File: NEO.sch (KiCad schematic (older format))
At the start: 13 parts, among them Q601 2N7002BKT, U601 U-BLOX-NEO-M8N, X601 ANT

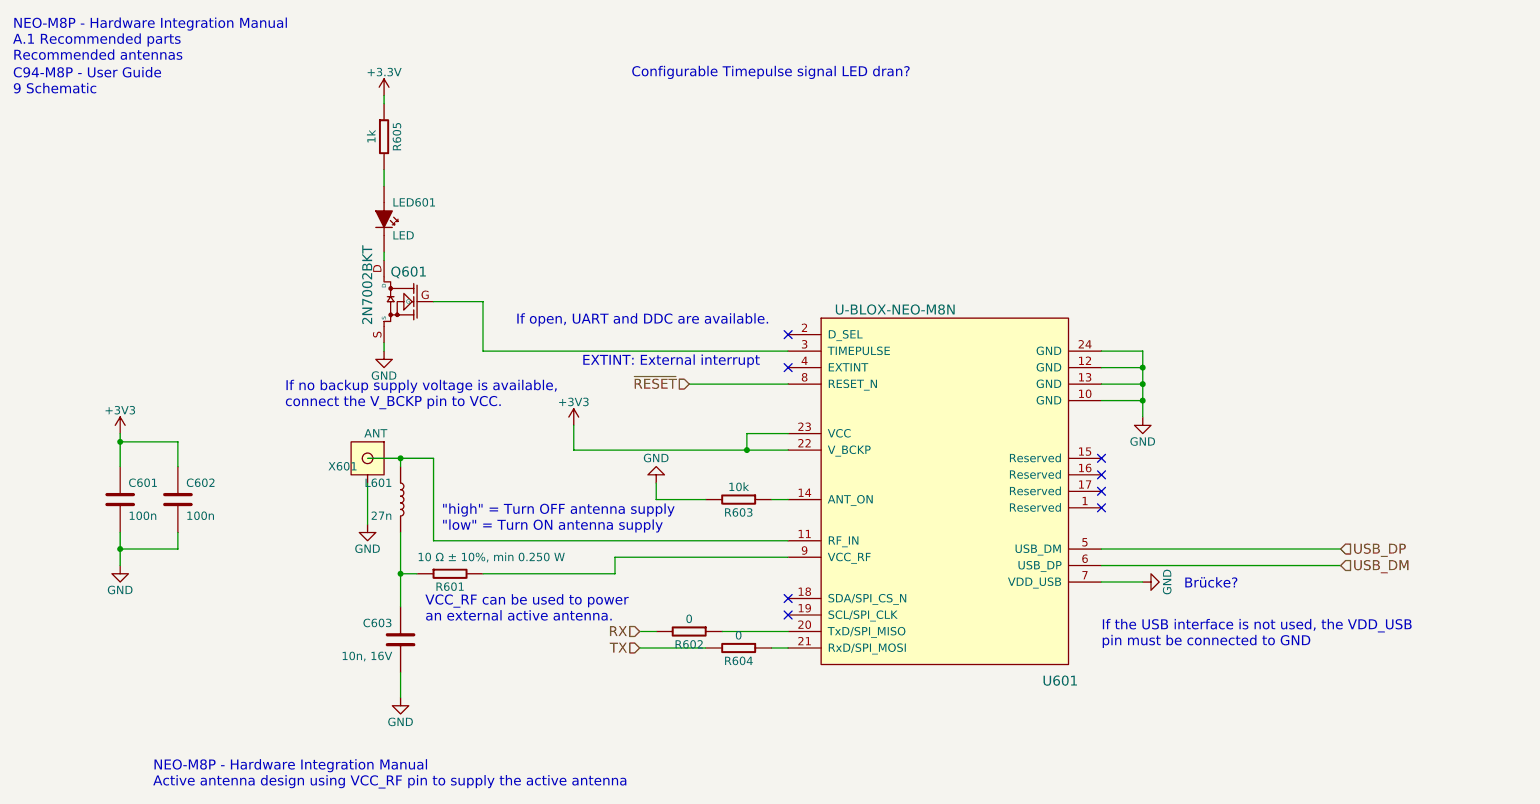
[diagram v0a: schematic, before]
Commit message: adjusted 3d models
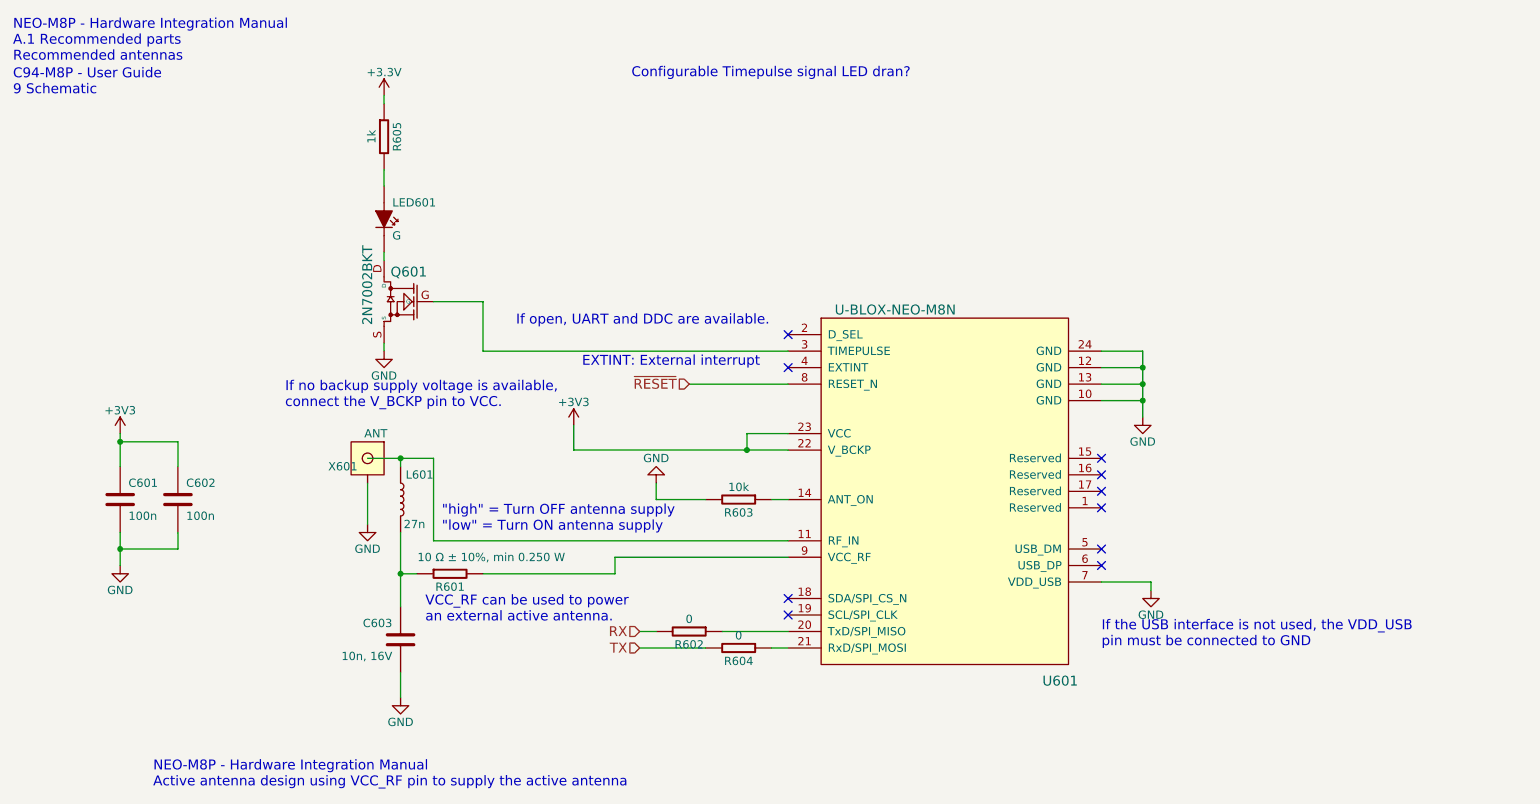
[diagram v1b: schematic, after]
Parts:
- LED601: value LED -> G; footprint (none) -> Passives:LED0603N
- Q601: footprint (none) -> Transistor:SOT416_GSD
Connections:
- net USB_DM: no longer names the net of U601.6 (USB_DP)
- net USB_DP: no longer names the net of U601.5 (USB_DM)
- no-connect marks 8 -> 10
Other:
- note removed: "Brücke?"
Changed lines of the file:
@@
 	3950 3100 3950 2950
 $Comp
-L +3V3 #PWR607
+L +3V3 #PWR0133
 U 1 1 57190E14
 P 3950 2950
-F 0 "#PWR607" H 3950 2800 50  0001 C CNN
+F 0 "#PWR0133" H 3950 2800 50  0001 C CNN
 F 1 "+3V3" H 3950 3090 50  0000 C CNN
 F 2 "" H 3950 2950 50  0000 C CNN
@@
 $EndComp
 $Comp
-L GND #PWR609
+L GND #PWR0134
 U 1 1 57190E68
 P 7400 2900
-F 0 "#PWR609" H 7400 2650 50  0001 C CNN
+F 0 "#PWR0134" H 7400 2650 50  0001 C CNN
 F 1 "GND" H 7400 2750 50  0000 C CNN
 F 2 "" H 7400 2900 50  0000 C CNN
@@
 	5000 3000 5000 3100
 Connection ~ 5000 3100
-Wire Wire Line
-	7150 3700 8600 3700
-Wire Wire Line
-	7150 3800 8600 3800
-Text HLabel 8600 3700 2    60   Input ~ 0
-USB_DP
-Text HLabel 8600 3800 2    60   Input ~ 0
-USB_DM
 $Comp
 L R R602
@@
 U 1 1 571915BF
 P 2900 3400
-F 0 "L601" H 2950 3500 50  0000 L CNN
-F 1 "27n" H 2950 3300 50  0000 L CNN
+F 0 "L601" H 2700 3550 50  0000 L CNN
+F 1 "27n" H 2750 3250 50  0000 L CNN
 F 2 "Passives:L0402N" H 2938 3250 30  0001 C CNN
 F 3 "LQG15HS27NJ02" H 2900 3400 60  0001 C CNN
@@
 Connection ~ 2900 3850
 $Comp
-L GND #PWR606
+L GND #PWR0135
 U 1 1 57191865
 P 2900 4600
-F 0 "#PWR606" H 2900 4350 50  0001 C CNN
+F 0 "#PWR0135" H 2900 4350 50  0001 C CNN
 F 1 "GND" H 2900 4450 50  0000 C CNN
 F 2 "" H 2900 4600 50  0000 C CNN
@@
 $EndComp
 $Comp
-L GND #PWR603
+L GND #PWR0136
 U 1 1 57191891
 P 2700 3550
-F 0 "#PWR603" H 2700 3300 50  0001 C CNN
+F 0 "#PWR0136" H 2700 3300 50  0001 C CNN
 F 1 "GND" H 2700 3400 50  0000 C CNN
 F 2 "" H 2700 3550 50  0000 C CNN
@@
 Text Notes 7150 4300 0    60   ~ 0
 If the USB interface is not used, the VDD_USB \npin must be connected to GND
-$Comp
-L GND #PWR610
-U 1 1 57211386
-P 7400 3900
-F 0 "#PWR610" H 7400 3650 50  0001 C CNN
-F 1 "GND" H 7400 3750 50  0000 C CNN
-F 2 "" H 7400 3900 50  0000 C CNN
-F 3 "" H 7400 3900 50  0000 C CNN
-	1    7400 3900
-	0    -1   -1   0
-$EndComp
-Wire Wire Line
-	7150 3900 7400 3900
-Text Notes 7650 3950 0    60   ~ 0
-Brücke?
 Text Notes 3150 3600 0    60   ~ 0
 "high" = Turn OFF antenna supply\n"low" = Turn ON antenna supply \n
@@
 $EndComp
 $Comp
-L GND #PWR608
+L GND #PWR0137
 U 1 1 57211964
 P 4450 3300
-F 0 "#PWR608" H 4450 3050 50  0001 C CNN
+F 0 "#PWR0137" H 4450 3050 50  0001 C CNN
 F 1 "GND" H 4450 3150 50  0000 C CNN
 F 2 "" H 4450 3300 50  0000 C CNN
@@
 $EndComp
 $Comp
-L +3V3 #PWR601
+L +3V3 #PWR0138
 U 1 1 57260BFE
 P 1200 3000
-F 0 "#PWR601" H 1200 2850 50  0001 C CNN
+F 0 "#PWR0138" H 1200 2850 50  0001 C CNN
 F 1 "+3V3" H 1200 3140 50  0000 C CNN
 F 2 "" H 1200 3000 50  0000 C CNN
@@
 $EndComp
 $Comp
-L GND #PWR602
+L GND #PWR0139
 U 1 1 57260C27
 P 1200 3800
-F 0 "#PWR602" H 1200 3550 50  0001 C CNN
+F 0 "#PWR0139" H 1200 3550 50  0001 C CNN
 F 1 "GND" H 1200 3650 50  0000 C CNN
 F 2 "" H 1200 3800 50  0000 C CNN
@@
 P 2800 1700
 F 0 "LED601" H 2850 1800 50  0000 L CNN
-F 1 "LED" H 2850 1600 50  0000 L CNN
-F 2 "" H 2838 1550 30  0001 C CNN
+F 1 "G" H 2850 1600 50  0000 L CNN
+F 2 "Passives:LED0603N" H 2838 1550 30  0001 C CNN
 F 3 "" H 2800 1700 60  0000 C CNN
 	1    2800 1700
@@
 F 0 "Q601" H 2650 2380 60  0000 C CNN
 F 1 "2N7002BKT" V 2900 2300 60  0000 C CNN
-F 2 "" H 2150 2525 60  0001 C CNN
+F 2 "Transistor:SOT416_GSD" H 2150 2525 60  0001 C CNN
 F 3 "" H 2150 2525 60  0000 C CNN
 	1    2800 2200
@@
 $EndComp
 $Comp
-L GND #PWR605
+L GND #PWR0140
 U 1 1 572B35D6
 P 2800 2500
-F 0 "#PWR605" H 2800 2250 50  0001 C CNN
+F 0 "#PWR0140" H 2800 2250 50  0001 C CNN
 F 1 "GND" H 2800 2350 50  0000 C CNN
 F 2 "" H 2800 2500 50  0000 C CNN
@@
 	2800 1400 2800 1500
 $Comp
-L +3.3V #PWR604
+L +3.3V #PWR0141
 U 1 1 572B3723
 P 2800 950
-F 0 "#PWR604" H 2800 800 50  0001 C CNN
+F 0 "#PWR0141" H 2800 800 50  0001 C CNN
 F 1 "+3.3V" H 2800 1090 50  0000 C CNN
 F 2 "" H 2800 950 50  0000 C CNN
@@
 Wire Wire Line
 	3400 2500 5250 2500
+$Comp
+L GND #PWR0142
+U 1 1 572CC1B5
+P 7450 3950
+F 0 "#PWR0142" H 7450 3700 50  0001 C CNN
+F 1 "GND" H 7450 3800 50  0000 C CNN
+F 2 "" H 7450 3950 50  0000 C CNN
+F 3 "" H 7450 3950 50  0000 C CNN
+	1    7450 3950
+	1    0    0    -1
+$EndComp
+Wire Wire Line
+	7150 3900 7450 3900
+Wire Wire Line
+	7450 3900 7450 3950
+NoConn ~ 7150 3800
+NoConn ~ 7150 3700
 $EndSCHEMATC

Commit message: sorted components
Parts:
- added R606: 10, Passives:R0402N, symbol R
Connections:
- net at U601.3 (TIMEPULSE): now also R606.1; no longer Q601.G
- new net: Q601.G, R606.2
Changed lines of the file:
@@
 	3950 3100 3950 2950
 $Comp
-L +3V3 #PWR0133
+L +3V3 #PWR607
 U 1 1 57190E14
 P 3950 2950
-F 0 "#PWR0133" H 3950 2800 50  0001 C CNN
+F 0 "#PWR607" H 3950 2800 50  0001 C CNN
 F 1 "+3V3" H 3950 3090 50  0000 C CNN
 F 2 "" H 3950 2950 50  0000 C CNN
@@
 $EndComp
 $Comp
-L GND #PWR0134
+L GND #PWR609
 U 1 1 57190E68
 P 7400 2900
-F 0 "#PWR0134" H 7400 2650 50  0001 C CNN
+F 0 "#PWR609" H 7400 2650 50  0001 C CNN
 F 1 "GND" H 7400 2750 50  0000 C CNN
 F 2 "" H 7400 2900 50  0000 C CNN
@@
 Connection ~ 2900 3850
 $Comp
-L GND #PWR0135
+L GND #PWR606
 U 1 1 57191865
 P 2900 4600
-F 0 "#PWR0135" H 2900 4350 50  0001 C CNN
+F 0 "#PWR606" H 2900 4350 50  0001 C CNN
 F 1 "GND" H 2900 4450 50  0000 C CNN
 F 2 "" H 2900 4600 50  0000 C CNN
@@
 $EndComp
 $Comp
-L GND #PWR0136
+L GND #PWR603
 U 1 1 57191891
 P 2700 3550
-F 0 "#PWR0136" H 2700 3300 50  0001 C CNN
+F 0 "#PWR603" H 2700 3300 50  0001 C CNN
 F 1 "GND" H 2700 3400 50  0000 C CNN
 F 2 "" H 2700 3550 50  0000 C CNN
@@
 $EndComp
 $Comp
-L GND #PWR0137
+L GND #PWR608
 U 1 1 57211964
 P 4450 3300
-F 0 "#PWR0137" H 4450 3050 50  0001 C CNN
+F 0 "#PWR608" H 4450 3050 50  0001 C CNN
 F 1 "GND" H 4450 3150 50  0000 C CNN
 F 2 "" H 4450 3300 50  0000 C CNN
@@
 $EndComp
 $Comp
-L +3V3 #PWR0138
+L +3V3 #PWR601
 U 1 1 57260BFE
 P 1200 3000
-F 0 "#PWR0138" H 1200 2850 50  0001 C CNN
+F 0 "#PWR601" H 1200 2850 50  0001 C CNN
 F 1 "+3V3" H 1200 3140 50  0000 C CNN
 F 2 "" H 1200 3000 50  0000 C CNN
@@
 $EndComp
 $Comp
-L GND #PWR0139
+L GND #PWR602
 U 1 1 57260C27
 P 1200 3800
-F 0 "#PWR0139" H 1200 3550 50  0001 C CNN
+F 0 "#PWR602" H 1200 3550 50  0001 C CNN
 F 1 "GND" H 1200 3650 50  0000 C CNN
 F 2 "" H 1200 3800 50  0000 C CNN
@@
 $EndComp
 $Comp
-L GND #PWR0140
+L GND #PWR605
 U 1 1 572B35D6
 P 2800 2500
-F 0 "#PWR0140" H 2800 2250 50  0001 C CNN
+F 0 "#PWR605" H 2800 2250 50  0001 C CNN
 F 1 "GND" H 2800 2350 50  0000 C CNN
 F 2 "" H 2800 2500 50  0000 C CNN
@@
 	2800 1400 2800 1500
 $Comp
-L +3.3V #PWR0141
+L +3.3V #PWR604
 U 1 1 572B3723
 P 2800 950
-F 0 "#PWR0141" H 2800 800 50  0001 C CNN
+F 0 "#PWR604" H 2800 800 50  0001 C CNN
 F 1 "+3.3V" H 2800 1090 50  0000 C CNN
 F 2 "" H 2800 950 50  0000 C CNN
@@
 Wire Wire Line
 	3400 2200 3400 2500
-Wire Wire Line
-	3400 2500 5250 2500
-$Comp
-L GND #PWR0142
+$Comp
+L GND #PWR610
 U 1 1 572CC1B5
 P 7450 3950
-F 0 "#PWR0142" H 7450 3700 50  0001 C CNN
+F 0 "#PWR610" H 7450 3700 50  0001 C CNN
 F 1 "GND" H 7450 3800 50  0000 C CNN
 F 2 "" H 7450 3950 50  0000 C CNN
@@
 NoConn ~ 7150 3800
 NoConn ~ 7150 3700
+$Comp
+L R R606
+U 1 1 572F007B
+P 3600 2500
+F 0 "R606" V 3680 2500 50  0000 C CNN
+F 1 "10" V 3525 2500 50  0000 C CNN
+F 2 "Passives:R0402N" V 3530 2500 30  0001 C CNN
+F 3 "" H 3600 2500 30  0000 C CNN
+	1    3600 2500
+	0    1    1    0
+$EndComp
+Wire Wire Line
+	3800 2500 5250 2500
 $EndSCHEMATC
